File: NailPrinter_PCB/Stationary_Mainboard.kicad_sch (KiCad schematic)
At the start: 20 parts, among them J1 Conn_01x24, Q1 AO3401, Q2 AO3401, U1 AO3400, U2 AO3400, U3 CD4504BM

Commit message: mostly schematic and pcb design
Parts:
- removed C1, C2, C3, C4: 10n, symbol Device:C
- removed C5, C6: 100n, symbol Device:C
- removed J1: Conn_01x24, symbol Connector_Generic:Conn_01x24
- removed Q1, Q2: AO3401, AO3401:SOT23, symbol AO3401:AO3401
- removed R1, R8: 2.7, symbol Device:R
- removed R2, R4, R6, R7: 1k, symbol Device:R
- removed R3, R5: 10k, symbol Device:R
- removed U1, U2: AO3400, AO3400:SOT23, symbol AO3400:AO3400
- removed U3: CD4504BM, CD4504BM:SOIC127P600X175-16N, symbol CD4504BM:CD4504BM
- added C1, C2: 100uF, Capacitor_THT:CP_Radial_D6.3mm_P2.50mm, symbol Device:C_Polarized
- added F1: Fuse, Fuse:FuseHolder_Blade_ATO_Littelfuse_FLR_178.6165, symbol Device:Fuse
- added J1: Barrel_Jack, Connector_BarrelJack:BarrelJack_Horizontal, symbol Connector:Barrel_Jack
- added J2: Conn_01x03, Connector_JST:JST_XH_B3B-XH-AM_1x03_P2.50mm_Vertical, symbol Connector_Generic:Conn_01x03
- added J3, J4, J5, J6, J8: Conn_01x04, Connector_JST:JST_XH_B4B-XH-A_1x04_P2.50mm_Vertical, symbol Connector_Generic:Conn_01x04
- added J7: Conn_01x03, Connector_JST:JST_XH_B3B-XH-A_1x03_P2.50mm_Vertical, symbol Connector_Generic:Conn_01x03
- added J9: Conn_01x24, Connector_IDC:IDC-Header_2x12_P2.54mm_Vertical, symbol Connector_Generic:Conn_01x24
- added R10, R11, R12, R13, R14, R15, R16, R17, R18, R9: 22, symbol Device:R
- added SW1: SW_SPST, Connector_PinHeader_2.54mm:PinHeader_1x03_P2.54mm_Vertical, symbol Switch:SW_SPST
- added U1: DEVKIT_V1_ESP32-WROOM-32, NailPrinter_Parts:MODULE_DEVKIT_V1_ESP32-WROOM-32, symbol DEVKIT_V1_ESP32-WROOM-32:DEVKIT_V1_ESP32-WROOM-32
- added U_TMC_X1, U_TMC_Y1: BTT_TMC2209_V1.2, Module:Pololu_Breakout-16_15.2x20.3mm, symbol TMC2208_SILENTSTEPSTICK:TMC2208_SILENTSTEPSTICK
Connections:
- net +16V: now also J4.3 (Pin_3), J9.1 (Pin_1), J9.2 (Pin_2), J9.3 (Pin_3)
- net +3.3V: now also J2.1 (Pin_1), J9.19 (Pin_19), U1.1 (3V3), U_TMC_X1.10 (VIO), U_TMC_Y1.10 (VIO)
- net +9V: now also J5.3 (Pin_3), J9.8 (Pin_8)
- net CLK_3V: now also R10.1, U1.15 (IO23)
- net D1_3V: now also R11.1, U1.14 (IO22)
- net D2_3V: now also R12.1, U1.11 (IO21)
- net D3_3V: now also R13.1, U1.10 (IO19)
- net ENC_A: now also J9.16 (Pin_16), U1.17 (SENSOR_VP)
- net ENC_B: now also J9.17 (Pin_17), U1.18 (SENSOR_VN)
- net GND: now also C1.2, C2.2, J1.2, J2.3 (Pin_3), J4.2 (Pin_2), J4.4 (Pin_4), J5.2 (Pin_2), J5.4 (Pin_4), J6.2 (Pin_2), J6.4 (Pin_4), J7.1 (Pin_1), J9.11 (Pin_11), J9.15 (Pin_15), J9.18 (Pin_18), J9.4 (Pin_4), J9.7 (Pin_7), U1.2 (GND1), U1.29 (GND2), U_TMC_X1.15 (GND), U_TMC_X1.9 (GND), U_TMC_Y1.15 (GND), U_TMC_Y1.9 (GND)
- net PWRA_IN: now also J9.6 (Pin_6), U1.25 (IO27)
- net PWRB_IN: now also J9.5 (Pin_5), U1.26 (IO14)
- net SYNC_3V: now also R9.1, U1.28 (IO13)
- new net: J9.20 (Pin_20), R14.2
- new net: J7.2 (Pin_2), U1.13 (TXD0)
- new net: J7.3 (Pin_3), U1.12 (RXD0)
- new net: J9.24 (Pin_24), R18.2
- new net: J9.23 (Pin_23), R17.2
- new net: J3.3 (Pin_3), U_TMC_X1.11 (OB1)
- new net: J3.1 (Pin_1), U_TMC_X1.12 (OA1)
- new net: J3.2 (Pin_2), U_TMC_X1.13 (OA2)
- new net: J3.4 (Pin_4), U_TMC_X1.14 (OB2)
- new net: F1.1, J1.1
- new net: F1.2, SW1.1 (A)
- new net: J8.1 (Pin_1), U_TMC_Y1.12 (OA1)
- new net: J8.2 (Pin_2), U_TMC_Y1.13 (OA2)
- new net: J8.3 (Pin_3), U_TMC_Y1.11 (OB1)
- new net: J8.4 (Pin_4), U_TMC_Y1.14 (OB2)
- new net: J9.21 (Pin_21), R15.2
- new net: J9.22 (Pin_22), R16.2
- new net +24V: C1.1, C2.1, J4.1 (Pin_1), J5.1 (Pin_1), J6.1 (Pin_1), SW1.2 (B), U_TMC_X1.16 (VM), U_TMC_Y1.16 (VM)
- new net +5V: J6.3 (Pin_3), U1.30 (EXT_5V)
- new net D4_3V: R14.1, U1.9 (IO18)
- new net D5_3V: R15.1, U1.8 (IO5)
- new net D6_3V: R16.1, U1.7 (IO17)
- new net D7_3V: R17.1, U1.6 (IO16)
- new net D8_3V: R18.1, U1.5 (IO4)
- new net DIAG_Y: U1.20 (IO35)
- new net DIR_X: U1.22 (IO33), U_TMC_X1.8 (DIR)
- new net DIR_Y: U1.24 (IO26), U_TMC_Y1.8 (DIR)
- new net ENDSTOP_X: J2.2 (Pin_2), U1.19 (IO34)
- new net EN_MOTORS: U1.27 (IO12), U_TMC_X1.1 (EN), U_TMC_Y1.1 (EN)
- new net STEP_X: U1.21 (IO32), U_TMC_X1.7 (STEP)
- new net STEP_Y: U1.23 (IO25), U_TMC_Y1.7 (STEP)
- new net UART_X: U_TMC_X1.4 (PDN/UART1)
- new net UART_Y: U1.3 (IO15), U_TMC_Y1.4 (PDN/UART1)
- no-connect marks 0 -> 13

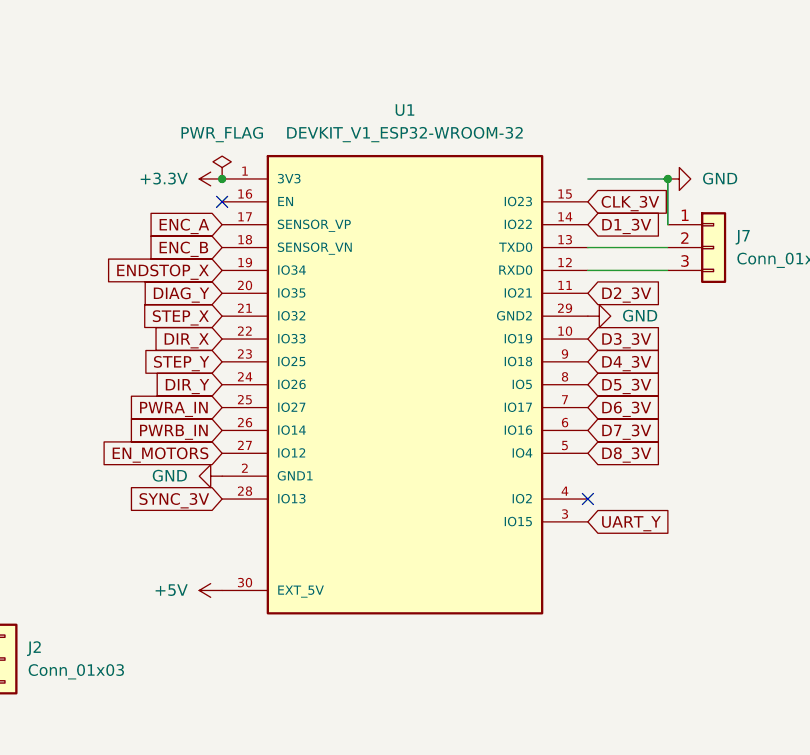
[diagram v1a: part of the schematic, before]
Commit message: Added TODO list to readme. Routed Mainboard PCB
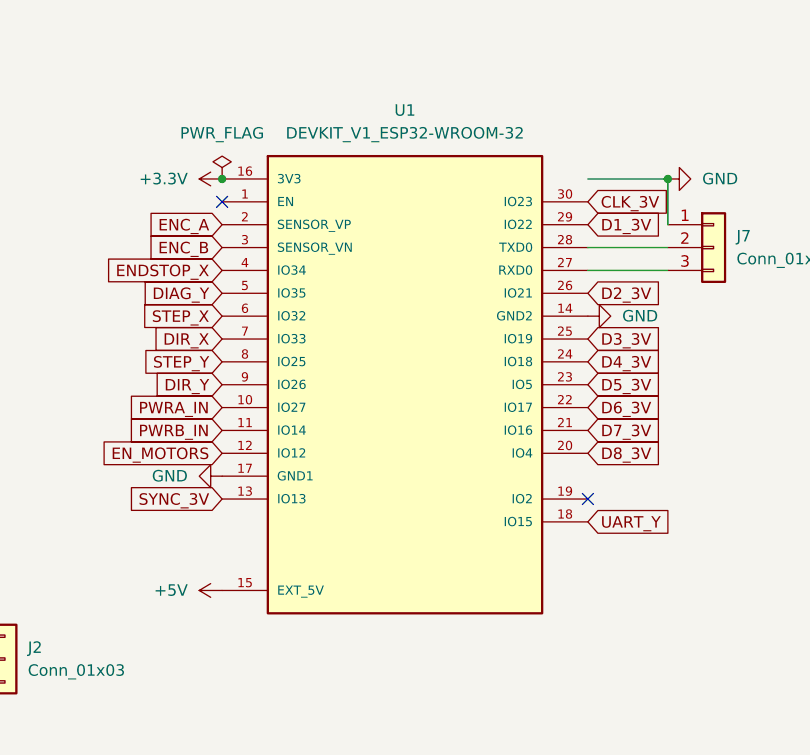
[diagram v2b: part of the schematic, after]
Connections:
- net +3.3V: now also U1.16 (3V3); no longer U1.1 (3V3)
- net +5V: now also U1.15 (EXT_5V); no longer U1.30 (EXT_5V)
- net CLK_3V: now also U1.30 (IO23); no longer U1.15 (IO23)
- net D1_3V: now also U1.29 (IO22); no longer U1.14 (IO22)
- net D2_3V: now also U1.26 (IO21); no longer U1.11 (IO21)
- net D3_3V: now also U1.25 (IO19); no longer U1.10 (IO19)
- net D4_3V: now also U1.24 (IO18); no longer U1.9 (IO18)
- net D5_3V: now also U1.23 (IO5); no longer U1.8 (IO5)
- net D6_3V: now also U1.22 (IO17); no longer U1.7 (IO17)
- net D7_3V: now also U1.21 (IO16); no longer U1.6 (IO16)
- net D8_3V: now also U1.20 (IO4); no longer U1.5 (IO4)
- net DIAG_Y: now also U1.5 (IO35); no longer U1.20 (IO35)
- net DIR_X: now also U1.7 (IO33); no longer U1.22 (IO33)
- net DIR_Y: now also U1.9 (IO26); no longer U1.24 (IO26)
- net ENC_A: now also U1.2 (SENSOR_VP); no longer U1.17 (SENSOR_VP)
- net ENC_B: now also U1.3 (SENSOR_VN); no longer U1.18 (SENSOR_VN)
- net ENDSTOP_X: now also U1.4 (IO34); no longer U1.19 (IO34)
- net EN_MOTORS: now also U1.12 (IO12); no longer U1.27 (IO12)
- net GND: now also U1.14 (GND2), U1.17 (GND1); no longer U1.2 (GND1), U1.29 (GND2)
- net PWRA_IN: now also U1.10 (IO27); no longer U1.25 (IO27)
- net PWRB_IN: now also U1.11 (IO14); no longer U1.26 (IO14)
- net STEP_X: now also U1.6 (IO32); no longer U1.21 (IO32)
- net STEP_Y: now also U1.8 (IO25); no longer U1.23 (IO25)
- net SYNC_3V: now also U1.13 (IO13); no longer U1.28 (IO13)
- net UART_Y: now also U1.18 (IO15); no longer U1.3 (IO15)
- net at J7.2 (Pin_2): now also U1.28 (TXD0); no longer U1.13 (TXD0)
- net at J7.3 (Pin_3): now also U1.27 (RXD0); no longer U1.12 (RXD0)
